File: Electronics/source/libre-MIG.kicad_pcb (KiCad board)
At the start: 2 copper layers, 161.2 x 103.5 mm, 245 parts, among them J1 Conn_01x05, J10 Conn_01x03, J11 Conn_01x08, J12 Conn_01x08, J13 Conn_01x05, J14 Conn_01x03, J15 Conn_01x06, J16 Conn_01x02, J17 Conn_01x06, J18 Conn_01x03, J19 Conn_01x08, J2 Conn_01x03, J20 Conn_01x03, J21 Conn_01x08, J22 Conn_01x04, J3 Conn_01x03, J4 Conn_01x05, J5 Conn_01x05, J6 Conn_01x20, J7 Conn_01x20, J8 Conn_01x03, J9 Conn_01x03, P1 USB_C_Plug_USB2.0, SW1 SW_Push, SW10 SW_Push, SW11 SW_Push, SW12 SW_Push, SW13 SW_Push, SW14 SW_Coded, SW15 RKJXV1220, SW16 SW_Push, SW17 SKRHABE010, SW18 SKRHABE010, SW2 SW_Push, SW3 SW_Push, SW4 SW_Push, SW5 SW_SPDT, SW6 SW_SPDT, SW7 SW_SPDT, SW8 SW_Push, SW9 SW_Push, U1 STM32F072CBTx, U2 TCA9535PWR, U3 TCA9535PWR, U5 ADP122AUJZ-3.3-R7, U6 MAX11615EEE, Y1 ABL-8.000MHZ-B2

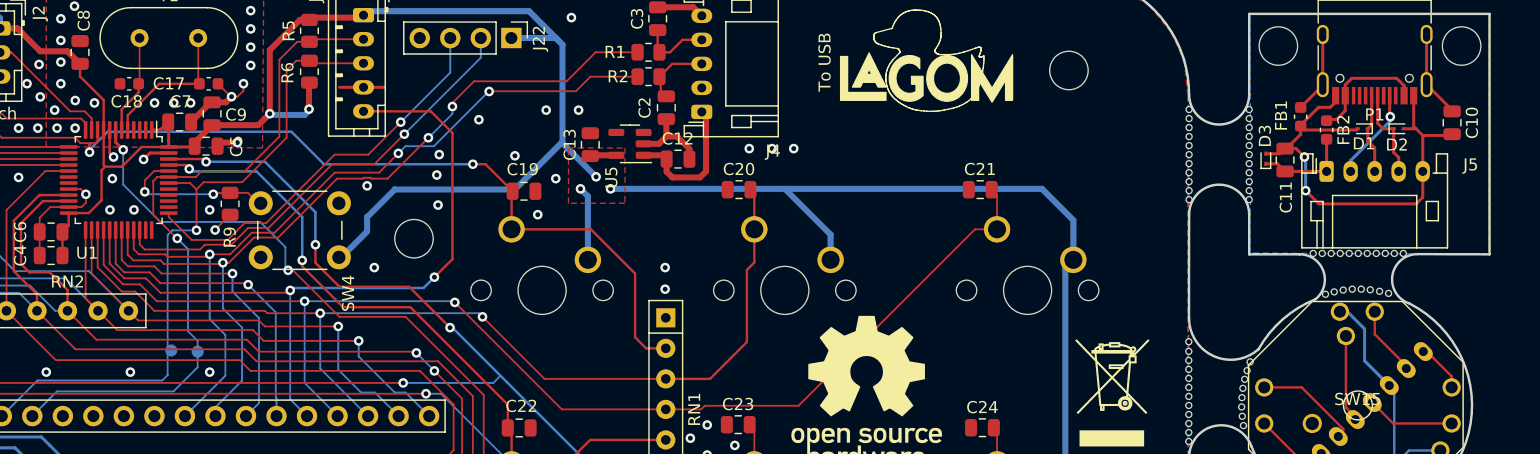
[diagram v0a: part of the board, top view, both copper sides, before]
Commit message: small bug fixes and clock stability
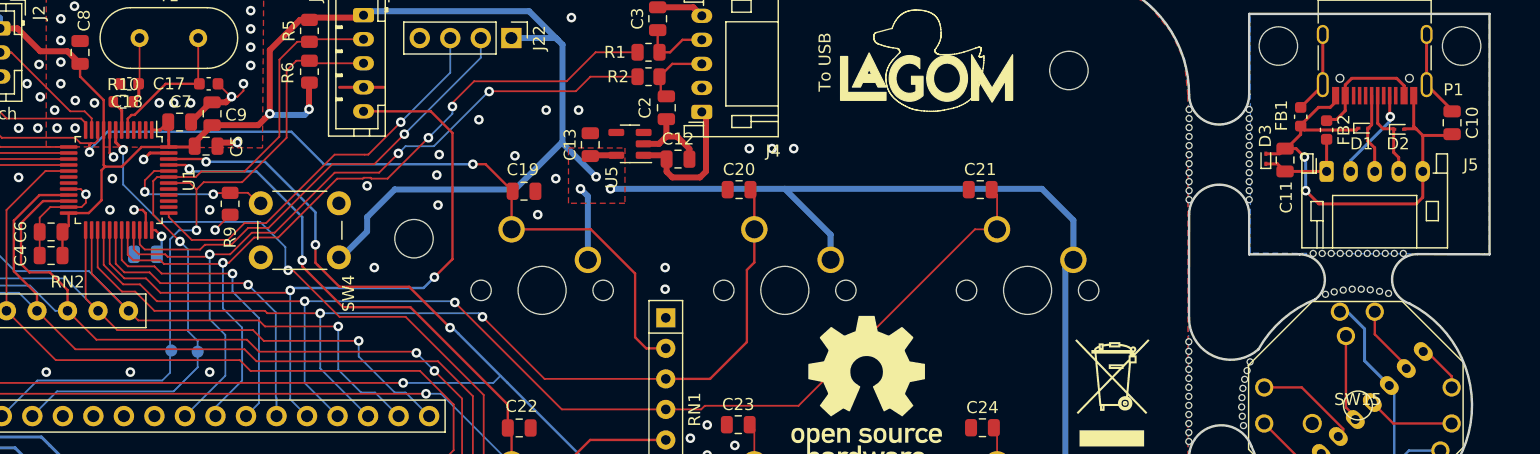
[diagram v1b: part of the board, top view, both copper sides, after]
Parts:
- added C1: 100nF, Capacitor_SMD:C_0805_2012Metric, B.Cu at (160.2, 126.3)
- added R10: 250, Resistor_SMD:R_0603_1608Metric, F.Cu at (158.3, 113.6)
- C17, C18: value 7pF -> 27pF
- D1, D2: value ESD9B3.3ST5G -> ESD9B5.0ST5G
- R5, R6: value 3k -> 5.6k
- moved D1 0.08 mm to (261.5, 115.8), turned to 0 degrees
- moved D2 0.06 mm to (264.5, 115.9)
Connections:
- D1 pad 1: Net-(D1-Pad1) -> GND
- D1 pad 2: GND -> Net-(J5-Pad3)
- J5 pad 3: Net-(D1-Pad1) -> Net-(J5-Pad3)
- P1 pad A7: Net-(D1-Pad1) -> Net-(J5-Pad3)
- U1 pad 1: +3V3 -> unconnected-(U1-Pad1)
- U1 pad 35: unconnected-(U1-Pad35) -> GND
- U1 pad 36: unconnected-(U1-Pad36) -> +3V3
- U1 pad 6: Net-(C18-Pad2) -> Net-(R10-Pad1)
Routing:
- net Net-(J5-Pad3): track 0.00 -> 6.68 mm
- net Net-(D1-Pad1): track 6.68 -> 0.00 mm
- net Net-(C18-Pad2): track 8.27 -> 5.53 mm
- net +3V3: track 649.7 -> 652.4 mm, vias 10 -> 11
- net Net-(R10-Pad1): track 0.00 -> 2.64 mm
- net GND: track 140.9 -> 143.4 mm

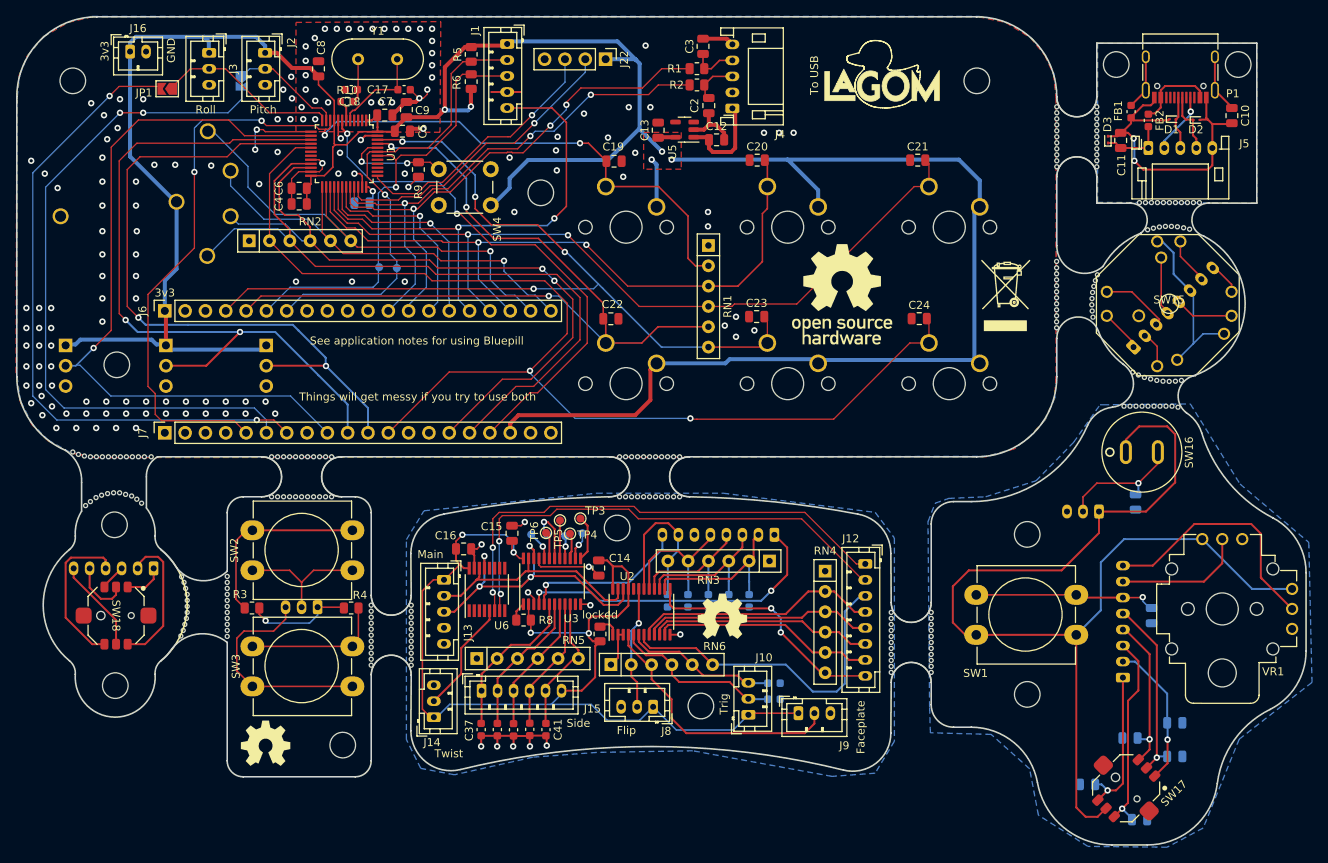
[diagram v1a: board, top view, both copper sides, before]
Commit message: added firmware submodule to firmware repo
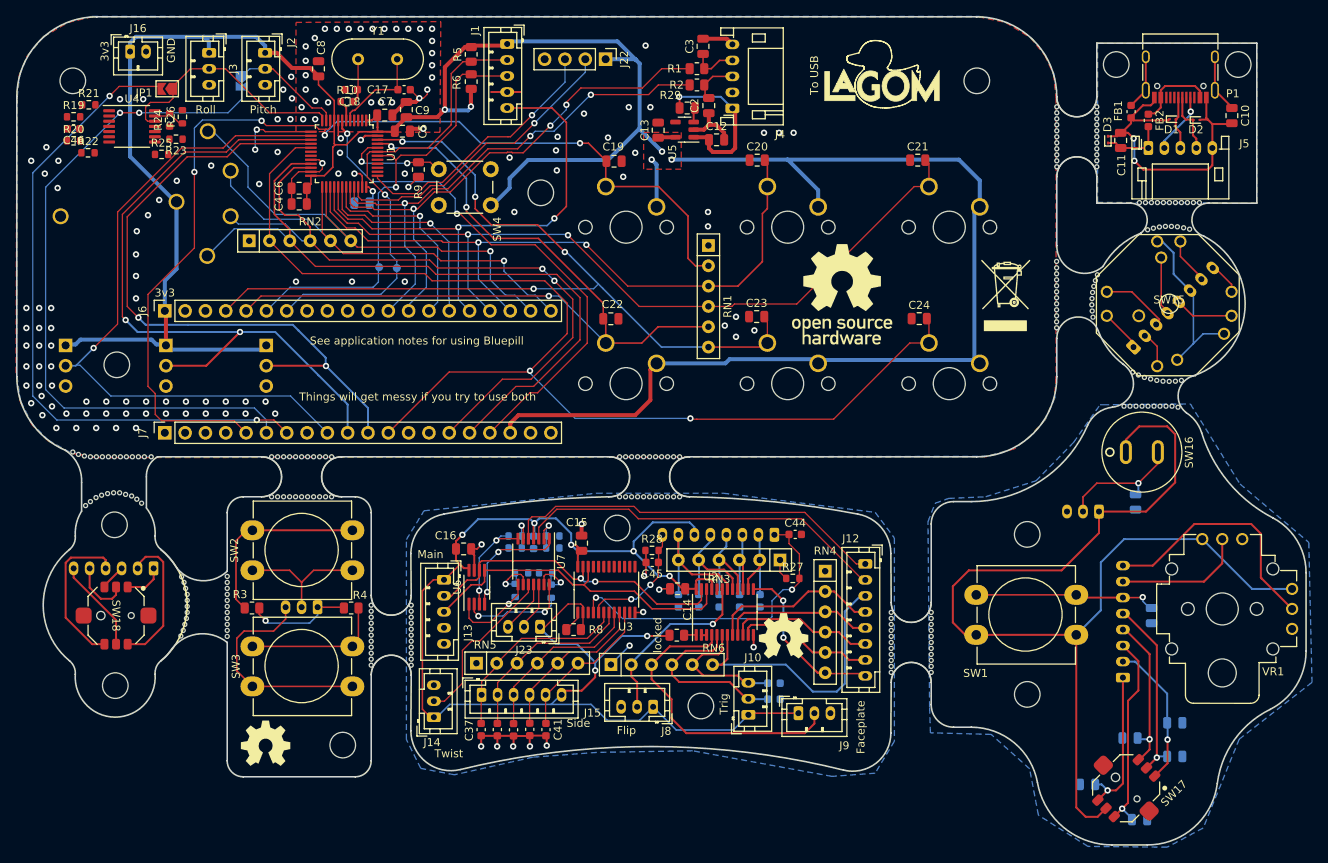
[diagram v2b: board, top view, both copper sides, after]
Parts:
- removed TP10, TP3, TP4, TP5, TP6, TP7, TP8, TP9: TestPoint, TestPoint:TestPoint_Pad_D1.0mm
- added C44: 10nF, Capacitor_SMD:C_0603_1608Metric, F.Cu at (214.3, 167.7)
- added C45: 10nF, Capacitor_SMD:C_0603_1608Metric, F.Cu at (196.4, 171.2)
- added C46: 100nF, Capacitor_SMD:C_0603_1608Metric, F.Cu at (124.1, 117.0)
- added C47: 100nF, Capacitor_SMD:C_0603_1608Metric, B.Cu at (181.6, 168.7)
- added J23: Conn_01x03, Connector_JST:JST_PH_B3B-PH-K_1x03_P2.00mm_Vertical, F.Cu at (182.4, 179.2)
- added R11: 10k, Resistor_SMD:R_0603_1608Metric, B.Cu at (180.1, 172.5)
- added R12: 10k, Resistor_SMD:R_0603_1608Metric, B.Cu at (183.1, 172.5)
- added R13: 7.96k, Resistor_SMD:R_0603_1608Metric, B.Cu at (179.3, 174.7)
- added R14: 7.96k, Resistor_SMD:R_0603_1608Metric, B.Cu at (183.8, 174.8)
- added R15: 10k, Resistor_SMD:R_0603_1608Metric, B.Cu at (179.3, 169.4)
- added R16: 10k, Resistor_SMD:R_0603_1608Metric, B.Cu at (184.0, 169.4)
- added R17: 7.96k, Resistor_SMD:R_0603_1608Metric, B.Cu at (179.3, 167.9)
- added R18: 7.96k, Resistor_SMD:R_0603_1608Metric, B.Cu at (184.0, 167.9)
- added R19: 10k, Resistor_SMD:R_0603_1608Metric, F.Cu at (124.1, 115.5)
- added R20: 10k, Resistor_SMD:R_0603_1608Metric, F.Cu at (124.1, 118.5)
- added R21: 7.96k, Resistor_SMD:R_0603_1608Metric, F.Cu at (126.0, 114.0)
- added R22: 7.96k, Resistor_SMD:R_0603_1608Metric, F.Cu at (125.9, 120.0)
- added R23: 10k, Resistor_SMD:R_0603_1608Metric, F.Cu at (136.9, 118.3)
- added R24: 10k, Resistor_SMD:R_0603_1608Metric, F.Cu at (136.1, 115.9)
- added R25: 7.96k, Resistor_SMD:R_0603_1608Metric, F.Cu at (135.1, 120.2)
- added R26: 7.96k, Resistor_SMD:R_0603_1608Metric, F.Cu at (137.7, 115.5)
- added R27: 620, Resistor_SMD:R_0603_1608Metric, F.Cu at (214.0, 173.2)
- added R28: 620, Resistor_SMD:R_0603_1608Metric, F.Cu at (196.4, 169.7)
- added R29: 10k, Capacitor_SMD:C_0805_2012Metric, F.Cu at (200.8, 114.4)
- added U4: LM2902, Package_SO:TSSOP-14_4.4x5mm_P0.65mm, F.Cu at (131.4, 116.7)
- added U7: LM2902, Package_SO:TSSOP-14_4.4x5mm_P0.65mm, F.Cu at (181.6, 171.1)
- RN1, RN2, RN3, RN4, RN5, RN6: value R_Network05 -> 10k
- U6: value MAX11615EEE -> MAX11613; footprint Package_SO:QSOP-16_3.9x4.9mm_P0.635mm -> Package_SO:MSOP-8_3x3mm_P0.65mm
- moved U2 10.4 mm to (205.5, 177.4)
- moved C14 10.2 mm to (199.6, 174.5), turned to 0 degrees
- moved locked 9.60 mm to (199.5, 180.3), turned to 180 degrees
- moved C15 8.79 mm to (187.6, 168.8)
- moved U3 6.88 mm to (190.7, 174.6)
- moved R8 6.37 mm to (186.6, 179.6)
- moved C25 1.36 mm to (204.8, 176.0)
- moved C33 1.36 mm to (207.3, 176.0)
- moved C34 1.36 mm to (202.2, 176.0)
- moved C35 1.36 mm to (199.7, 176.0)
- moved C36 1.36 mm to (209.9, 176.0)
- moved RN3 1.33 mm to (212.4, 170.9)
- moved U6 1.30 mm to (174.5, 174.3)
- moved RN5 0.59 mm to (174.4, 183.8)
- moved J15 0.51 mm to (175.1, 187.8)
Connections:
- J11 pad 6: GND -> +3V3
- J21 pad 6: GND -> +3V3
- SW15 pad C: GND -> +3V3
- U1 pad 11: /MCU/PitchIn -> /MCU/PitchAmp
- U1 pad 12: /MCU/RollIn -> /MCU/RollAmp
- U3 pad 13: /IO Controller/IN_xtra1 -> unconnected-(U3-Pad13)
- U3 pad 14: /IO Controller/IN_xtra2 -> unconnected-(U3-Pad14)
- U3 pad 15: /IO Controller/IN_xtra3 -> unconnected-(U3-Pad15)
- U3 pad 16: /IO Controller/IN_xtra4 -> unconnected-(U3-Pad16)
- U3 pad 17: /IO Controller/IN_xtra5 -> unconnected-(U3-Pad17)
- U3 pad 18: /IO Controller/IN_xtra6 -> unconnected-(U3-Pad18)
- U3 pad 19: /IO Controller/IN_xtra7 -> unconnected-(U3-Pad19)
- U3 pad 20: /IO Controller/IN_xtra8 -> unconnected-(U3-Pad20)
- U6 pad 1: unconnected-(U6-Pad1) -> /IO Controller/TwistAmp
- U6 pad 2: unconnected-(U6-Pad2) -> /IO Controller/BrakeAmp
- U6 pad 3: unconnected-(U6-Pad3) -> /IO Controller/Axis1Amp
- U6 pad 4: unconnected-(U6-Pad4) -> /IO Controller/Axis2Amp
- U6 pad 5: /IO Controller/TwistIn -> /IO Controller/SCL
- U6 pad 6: /IO Controller/Axis1 -> /IO Controller/SDA
- U6 pad 7: /IO Controller/Axis2 -> GND
- U6 pad 8: /IO Controller/AIN3 -> +3V3
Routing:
- net +3V3: track 652.4 -> 715.7 mm, vias 11 -> 14
- net GND: track 143.4 -> 123.4 mm, vias 153 -> 143
- net /IO Controller/BrakeAmp: track 0.00 -> 16.0 mm, vias 0 -> 2
- net /IO Controller/Axis2Amp: track 0.00 -> 14.7 mm, vias 0 -> 2
- net /IO Controller/Axis2: track 61.5 -> 46.8 mm, vias 2 -> 0
- net /IO Controller/Axis1: track 61.8 -> 48.1 mm, vias 2 -> 0
- net /IO Controller/Axis1Amp: track 0.00 -> 13.4 mm, vias 0 -> 2
- net /IO Controller/SDA: track 29.0 -> 41.1 mm, vias 0 -> 2
- net /IO Controller/TwistAmp: track 0.00 -> 12.0 mm, vias 0 -> 1
- net /IO Controller/DirU: track 27.8 -> 17.5 mm
- net /IO Controller/DirD: track 31.2 -> 21.2 mm
- net /IO Controller/DirR: track 28.0 -> 18.2 mm
- net /IO Controller/DirL: track 28.8 -> 19.1 mm
- net /IO Controller/DirC: track 30.8 -> 21.3 mm
- net /IO Controller/DirU1: track 20.6 -> 11.8 mm
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
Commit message: Added quick logo
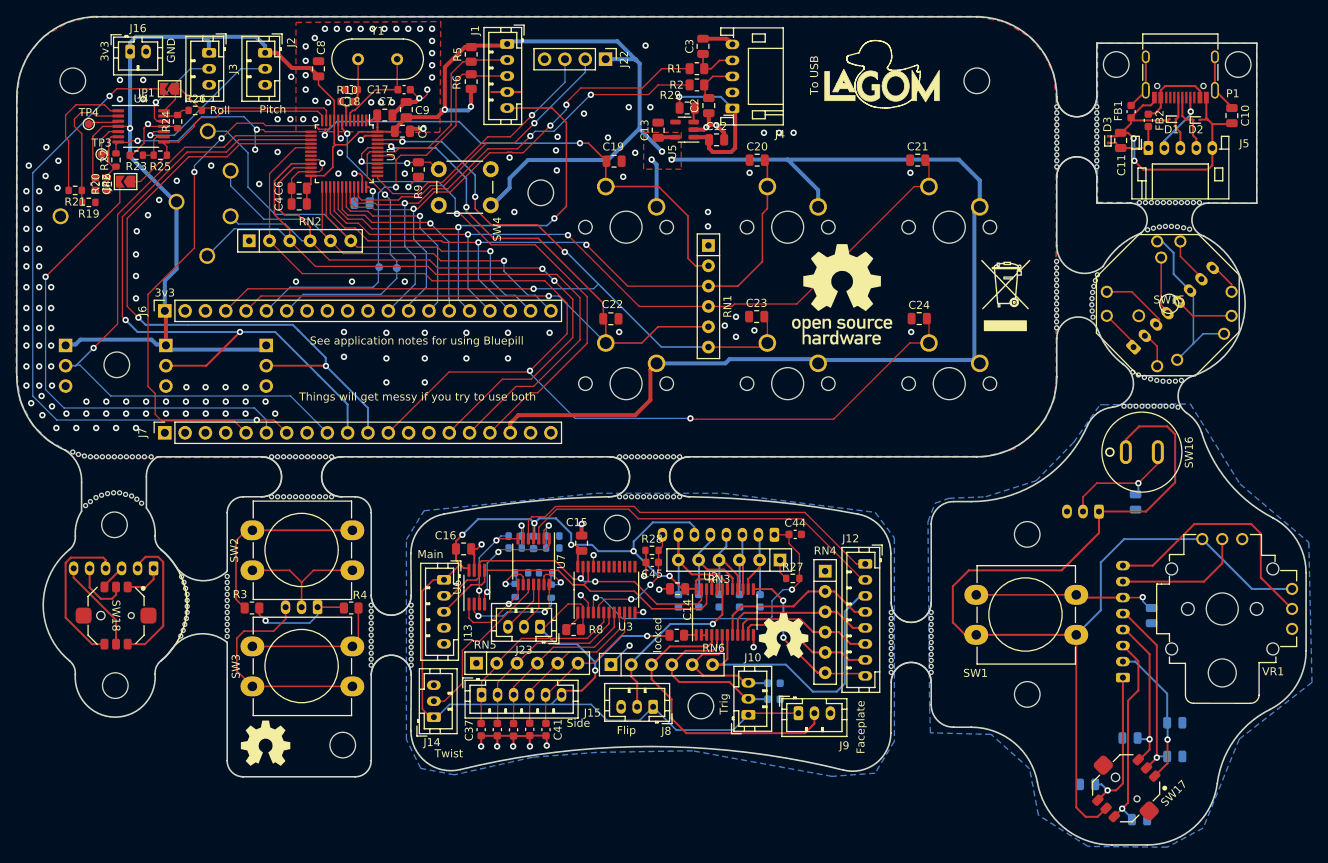
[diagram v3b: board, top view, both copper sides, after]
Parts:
- added TP3: TestPoint, TestPoint:TestPoint_Pad_D1.0mm, F.Cu at (127.6, 120.2)
- added TP4: TestPoint, TestPoint:TestPoint_Pad_D1.0mm, F.Cu at (126.0, 116.4)
- JP2: moved to F.Cu
- moved JP2 19.2 mm to (130.6, 123.6), turned to 180 degrees
- moved R19 10.9 mm to (126.0, 126.2), turned to 180 degrees
- moved R21 10.8 mm to (124.3, 124.7), turned to 180 degrees
- moved C46 7.41 mm to (126.8, 123.9), turned to -90 degrees
- moved R20 6.84 mm to (128.3, 123.9), turned to 90 degrees
- moved R23 5.35 mm to (131.9, 120.3), turned to 0 degrees
- moved R22 3.61 mm to (129.4, 120.9), turned to 90 degrees
- moved R26 1.79 mm to (139.3, 114.7), turned to 0 degrees
- moved U4 1.14 mm to (132.5, 116.7)
- moved R24 1.02 mm to (137.1, 116.1)
- moved JP1 0.30 mm to (136.1, 112.0)
- moved R25 0.19 mm to (134.9, 120.3), turned to 180 degrees
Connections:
- net /MCU/PitchIn2 renamed /MCU/PitchAmp2
- net /MCU/RollIn2 renamed /MCU/RollAmp2
- C46 pad 2: unconnected-(C46-Pad2) -> GND
- JP1 pad 1: /MCU/RollIn -> /MCU/RollAmp
- JP2 pad 1: /MCU/PitchIn -> /MCU/PitchAmp
- U1 pad 11: /MCU/PitchAmp -> /MCU/RollAmp
- U1 pad 12: /MCU/RollAmp -> /MCU/PitchAmp
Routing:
- net /MCU/PitchAmp: track 0.00 -> 30.0 mm
- net /MCU/PitchAmp2: track 86.7 -> 60.6 mm, vias 2 -> 1
- net /MCU/RollAmp: track 0.00 -> 24.8 mm
- net /MCU/ADC3: track 9.46 -> 30.3 mm, vias 2 -> 3
- net /MCU/RollIn: track 30.3 -> 11.8 mm, vias 0 -> 1
- net /MCU/ADC2: track 0.00 -> 17.0 mm
- net Net-(R19-Pad2): track 0.00 -> 16.8 mm
- net GND: track 123.4 -> 136.3 mm, vias 143 -> 181
- net +3V3: track 715.7 -> 726.3 mm, vias 14 -> 15
- net Net-(R20-Pad2): track 0.00 -> 7.12 mm
- net /MCU/PitchIn: track 14.1 -> 19.7 mm, vias 0 -> 1
- net Net-(R23-Pad2): track 0.00 -> 4.71 mm
- net /MCU/ADC3In: track 0.00 -> 4.37 mm
- net /MCU/ADC2In: track 0.00 -> 4.14 mm
- net /MCU/SW1: track 131.9 -> 128.8 mm
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
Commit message: corrected incomplete USB for flipable cable, and replaced termination resistors w jumpers
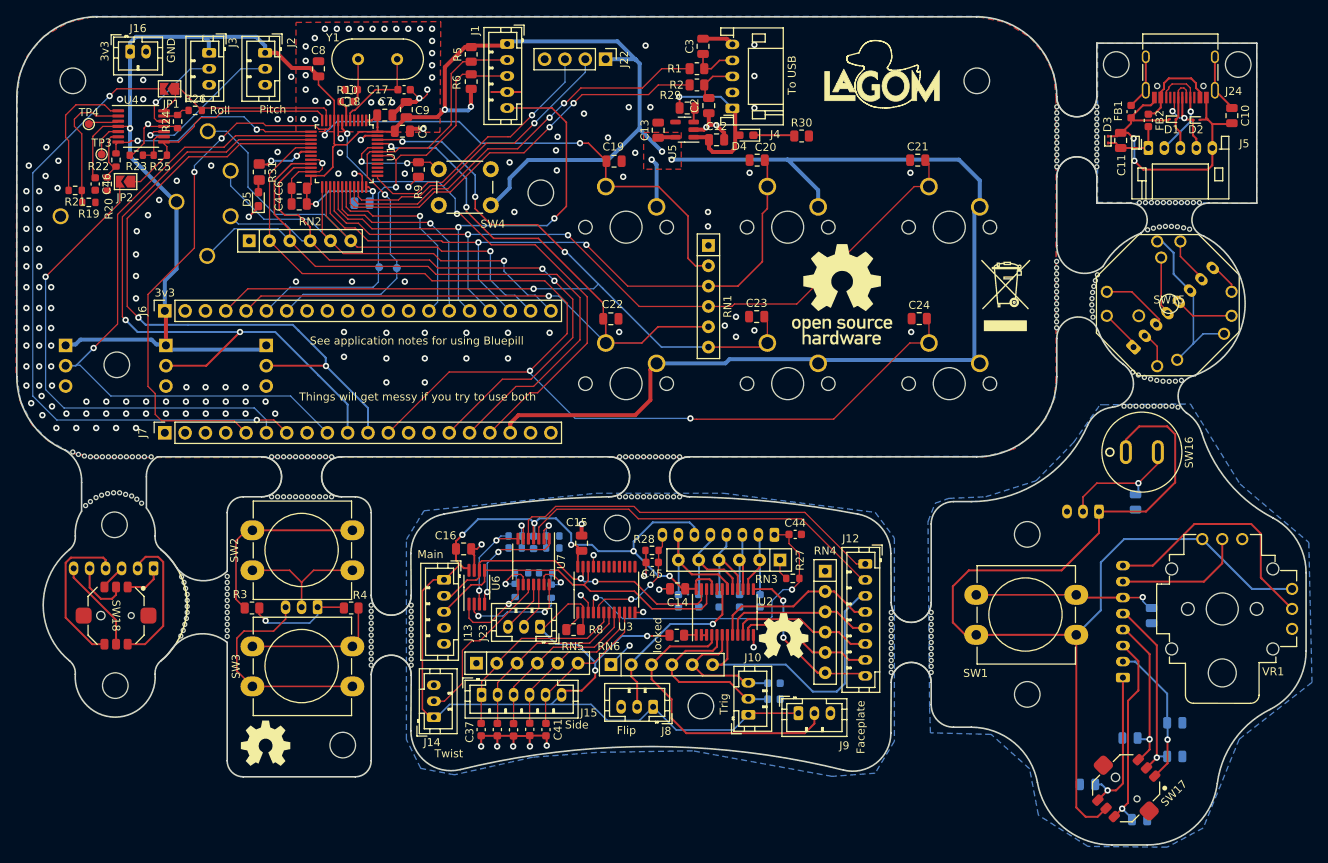
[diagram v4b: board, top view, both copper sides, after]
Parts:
- removed P1: USB_C_Plug_USB2.0, Connector_USB:USB_C_Receptacle_HRO_TYPE-C-31-M-12
- added D4: LED, LED_SMD:LED_0603_1608Metric_Pad1.05x0.95mm_HandSolder, F.Cu at (208.2, 117.8)
- added D5: LED, LED_SMD:LED_0603_1608Metric_Pad1.05x0.95mm_HandSolder, F.Cu at (147.2, 125.8)
- added J24: USB_C_Receptacle_USB2.0, Connector_USB:USB_C_Receptacle_HRO_TYPE-C-31-M-12, F.Cu at (262.4, 109.0)
- added R30: R, Resistor_SMD:R_0805_2012Metric, F.Cu at (215.1, 117.9)
- added R31: R, Resistor_SMD:R_0805_2012Metric_Pad1.20x1.40mm_HandSolder, F.Cu at (147.3, 122.4)
- R1, R2: value 27 -> 0
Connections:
- net Net-(C2-Pad1) renamed /MCU/ D-
- net Net-(C3-Pad1) renamed /MCU/D+
- net Net-(D1-Pad2) renamed /USB/D-
- net Net-(D2-Pad1) renamed /USB/D+
- R1 pad 1: /MCU/USB_DM -> /MCU/USB_DP
- R2 pad 2: /MCU/USB_DP -> /MCU/USB_DM
- U1 pad 18: unconnected-(U1-Pad18) -> /MCU/Error
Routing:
- net /MCU/USB_DM: track 67.0 -> 51.0 mm, vias 3 -> 2
- net /MCU/USB_DP: track 65.4 -> 50.7 mm, vias 3 -> 2
- net +3V3: track 726.3 -> 735.2 mm, vias 15 -> 16
- net /MCU/Error: track 0.00 -> 7.13 mm, vias 0 -> 2
- net Net-(J24-PadA5): track 7.69 -> 13.4 mm
- net Net-(D4-Pad1): track 0.00 -> 5.13 mm
- net /USB/D+: track 7.55 -> 11.2 mm, vias 0 -> 2
- net /USB/D-: track 6.68 -> 9.72 mm
- net /MCU/ADC3: track 30.3 -> 28.1 mm, vias 3 -> 2
- net GND: track 136.3 -> 138.1 mm
- net Net-(D5-Pad2): track 0.00 -> 1.63 mm
- net Net-(J24-PadA4): track 10.2 -> 11.6 mm
